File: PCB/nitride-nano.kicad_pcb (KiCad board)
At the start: 6 copper layers, 120 x 57 mm, 323 parts, among them J3 XT-90-M, J4 SWD, J5 SSD1306, J6 XT90-F, P1 USB_C_Plug_USB2.0, Q1 EPC2367, Q10 SQJB90EP-T1_GE3, Q11 AO3404A, Q12 HUASHUO HSBB0115, Q13 AO3404A, Q2 EPC2367, Q3 EPC2367, Q4 EPC2367, Q5 HUASHUO HSBB0115, Q6 AGM612AP, Q8 AO3404A, Q9 AO3404A, SW1 EC11E15244G1, U1 LT8390AIUFD-PBF, U10 SN74LVC1G17DBVR, U11 LMR16006XDDCR, U12 FT234XD, U13 LMR16006XDDCR, U2 STM32G474CEUx, U3 TPD4S480RUKR, U4 TPS26750SRSMR, U5 LM2765, U6 CAT24C512YI-GT3, U7 74LVC1G08SE-7, U8 LTC7004x, U9 INA228AIDGSR, Y1 8M

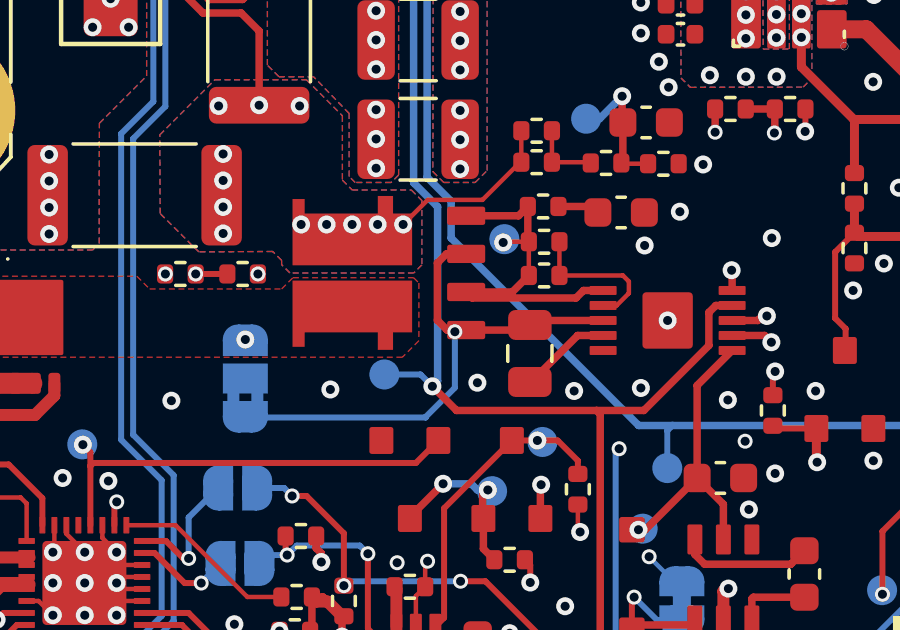
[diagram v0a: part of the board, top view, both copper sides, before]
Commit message: EPR sort of works with some chargers
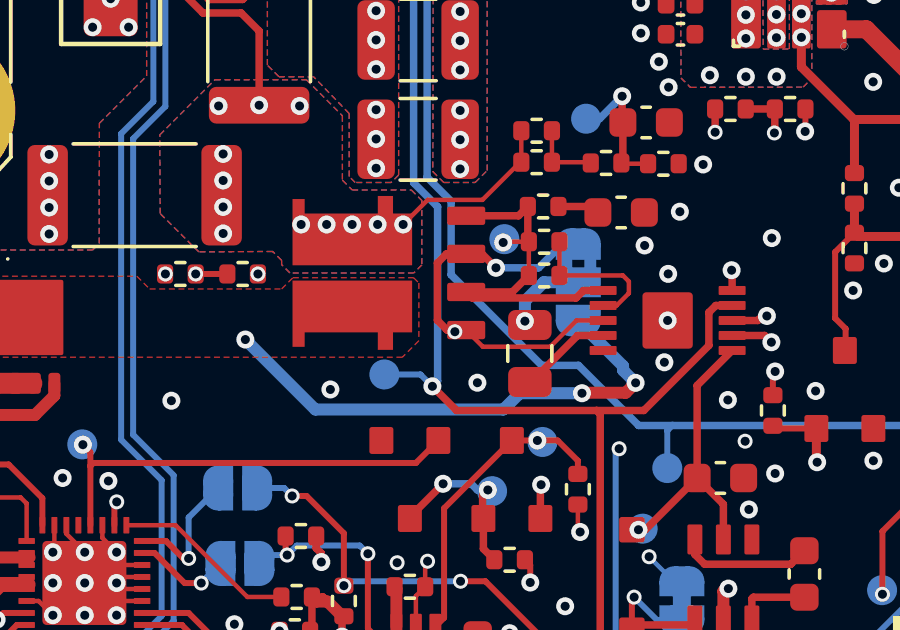
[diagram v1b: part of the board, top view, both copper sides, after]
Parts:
- R75, R76: value 10k -> 75k
- moved JP11 11.6 mm to (81.8, 103.3), turned to -90 degrees
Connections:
- C51 pad 1: /USB-PD/TS -> Net-(JP11-C)
- JP11 pad 2: /USB-PD/TS -> Net-(JP11-C)
- R75 pad 1: GND -> Net-(D20-K)
- R75 pad 2: Net-(D20-K) -> GND
- R76 pad 1: GND -> Net-(D21-K)
- R76 pad 2: Net-(D21-K) -> GND
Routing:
- net +VBUS: track 52.9 -> 70.1 mm, vias 3 -> 5
- net /USB-PD/TS: track 18.1 -> 13.5 mm, vias 1 -> 2
- net Net-(JP11-C): track 0.00 -> 2.71 mm, vias 0 -> 1
- net /MCU/SWITCH_EN_READ: track 69.8 -> 70.5 mm
